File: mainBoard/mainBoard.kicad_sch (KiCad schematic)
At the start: 22 parts, among them J1 Battery Output, J2 Programmer, J3 Keyboard, J4 display, M1 Vibration Motor, Q1 IRLML2502, U1 STM32G030K8Tx, U2 AMS1117-3.3, U3 W25Q128JVS, Y1 48MHz

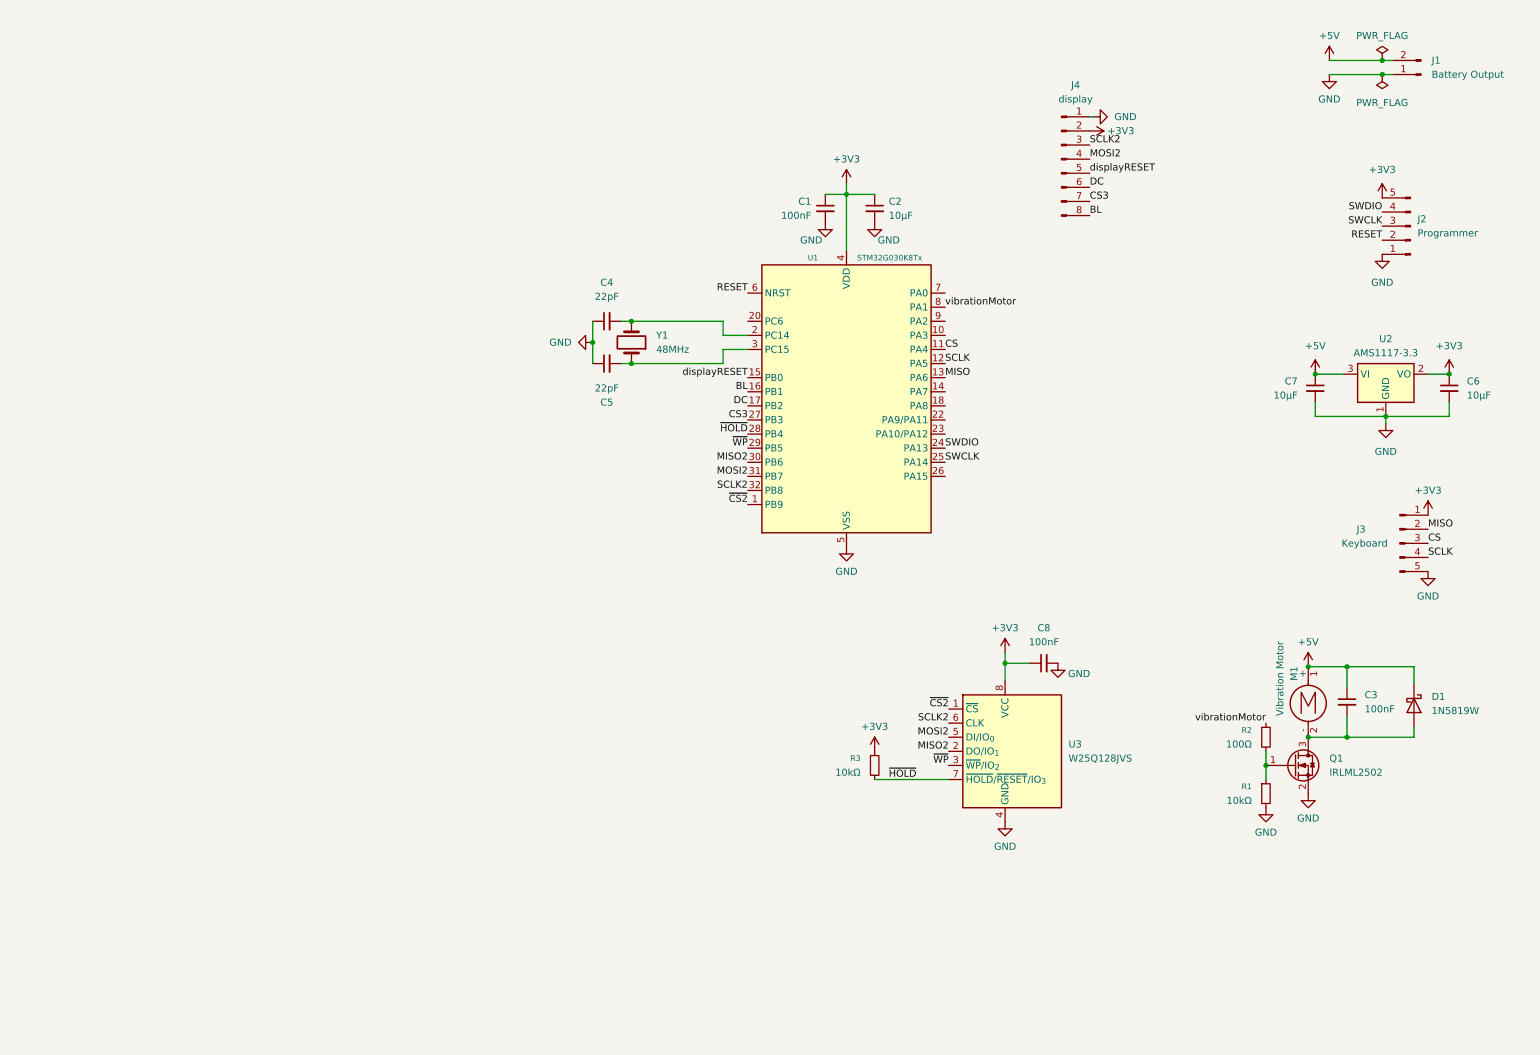
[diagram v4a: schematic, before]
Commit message: Routed PCB & fixed schematic issues
Added RYLR, added +5v to programmer headers, added caps to display, fixed rylr reset being connected to microcontroller reset.

Routed PCB
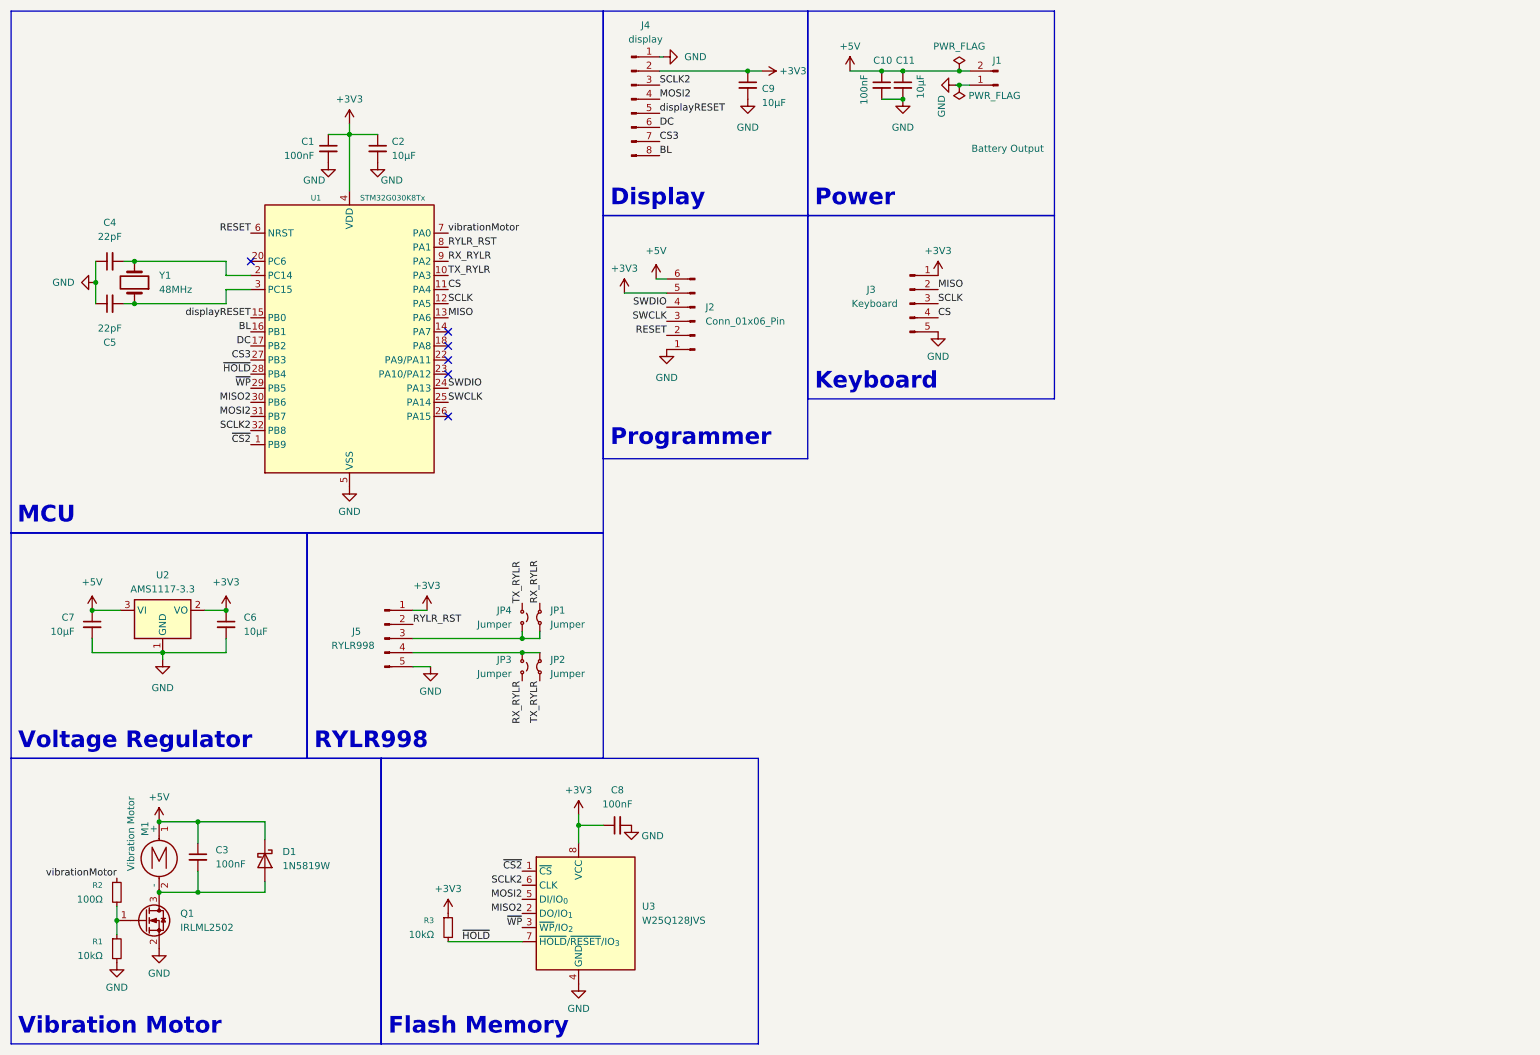
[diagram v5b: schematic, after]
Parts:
- removed J2: Programmer, symbol Connector:Conn_01x05_Pin
- added C10: 100nF, Capacitor_SMD:C_0603_1608Metric_Pad1.08x0.95mm_HandSolder, symbol Device:C_Small
- added C11, C9: 10µF, Capacitor_SMD:C_0603_1608Metric_Pad1.08x0.95mm_HandSolder, symbol Device:C_Small
- added J2: Conn_01x06_Pin, Connector_PinHeader_2.54mm:PinHeader_1x06_P2.54mm_Vertical, symbol Connector:Conn_01x06_Pin
- added J5: RYLR998, Connector_PinHeader_2.54mm:PinHeader_1x05_P2.54mm_Vertical, symbol Connector:Conn_01x05_Pin
- added JP1, JP2: Jumper, Jumper:SolderJumper-2_P1.3mm_Bridged_RoundedPad1.0x1.5mm, symbol Jumper:Jumper_2_Small_Bridged
- added JP3, JP4: Jumper, Jumper:SolderJumper-2_P1.3mm_Open_RoundedPad1.0x1.5mm, symbol Jumper:Jumper_2_Small_Open
- C1, C2, C3, C4, C5, C6, C7, C8: footprint (none) -> Capacitor_SMD:C_0603_1608Metric_Pad1.08x0.95mm_HandSolder
- J1, M1: footprint (none) -> Connector_PinHeader_2.54mm:PinHeader_1x02_P2.54mm_Vertical
- J3: footprint (none) -> Connector_PinHeader_2.54mm:PinHeader_1x05_P2.54mm_Vertical
- J4: footprint (none) -> Connector_PinHeader_2.54mm:PinHeader_1x08_P2.54mm_Vertical
- R1, R2, R3: footprint (none) -> Resistor_SMD:R_0603_1608Metric_Pad0.98x0.95mm_HandSolder
- Y1: footprint (none) -> Crystal:Crystal_HC49-U_Vertical
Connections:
- net +3V3: now also C9.1, J2.5 (Pin_5), J5.1 (Pin_1)
- net +5V: now also C10.1, C11.1, J2.6 (Pin_6)
- net CS: now also J3.4 (Pin_4); no longer J3.3 (Pin_3)
- net GND: now also C10.2, C11.2, C9.2, J2.1 (Pin_1), J5.5 (Pin_5)
- net RESET: now also J2.2 (Pin_2)
- net SCLK: now also J3.3 (Pin_3); no longer J3.4 (Pin_4)
- net SWCLK: now also J2.3 (Pin_3)
- net SWDIO: now also J2.4 (Pin_4)
- net vibrationMotor: now also U1.7 (PA0); no longer U1.8 (PA1)
- net TX_RYLR: now reaches U1.10 (PA3)
- net TX_RYLR: now also JP2.1 (A), JP4.2 (B)
- net RX_RYLR: now reaches U1.9 (PA2)
- net RX_RYLR: now also JP1.2 (B), JP3.1 (A)
- new net: J5.3 (Pin_3), JP1.1 (A), JP4.1 (A)
- new net: J5.4 (Pin_4), JP2.2 (B), JP3.2 (B)
- new net RYLR_RST: J5.2 (Pin_2), U1.8 (PA1)
- no-connect marks 0 -> 6
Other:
- note added: "Display"
- note added: "Flash Memory"
- note added: "Keyboard"
- note added: "MCU"
- note added: "Power"
- note added: "Programmer"
- note added: "RYLR998"
- note added: "Vibration Motor"
- note added: "Voltage Regulator"
- moved on the sheet: C1, C2, C3, C4, C5, C6, C7, C8, D1, J1, J3, J4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

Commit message: Fixed Minor Issue
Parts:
- removed C4, C5: 22pF, Capacitor_SMD:C_0603_1608Metric_Pad1.08x0.95mm_HandSolder, symbol Device:C_Small
- removed Y1: 48MHz, Crystal:Crystal_HC49-U_Vertical, symbol Device:Crystal
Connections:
- no-connect marks 6 -> 8

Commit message: Fixed minor issues & plotted gerber
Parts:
- added D2: Indicator LED, LED_SMD:LED_0603_1608Metric_Pad1.05x0.95mm_HandSolder, symbol Device:LED_Small
- added R4: 10kΩ, Resistor_SMD:R_0603_1608Metric_Pad0.98x0.95mm_HandSolder, symbol Device:R_Small
- added R5: 100Ω, Resistor_SMD:R_0603_1608Metric_Pad0.98x0.95mm_HandSolder, symbol Device:R_Small
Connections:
- net GND: now also R4.2, R5.2
- net SWCLK: now also R4.1
- net at U1.14 (PA7): now also D2.2 (A)
- new net: D2.1 (K), R5.1
- no-connect marks 8 -> 7
